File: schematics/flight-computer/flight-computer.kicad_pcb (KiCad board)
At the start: 4 copper layers, 80 x 80 mm, 141 parts, among them J101 BATT, J102 GPS, J103 TELEM, J104 Expansion Slot, J105 USB C, J106 SWD, J107 BLACKBOX, J301 BMI-S-201, Q101 BSS138, U101 STM32F405RGT6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

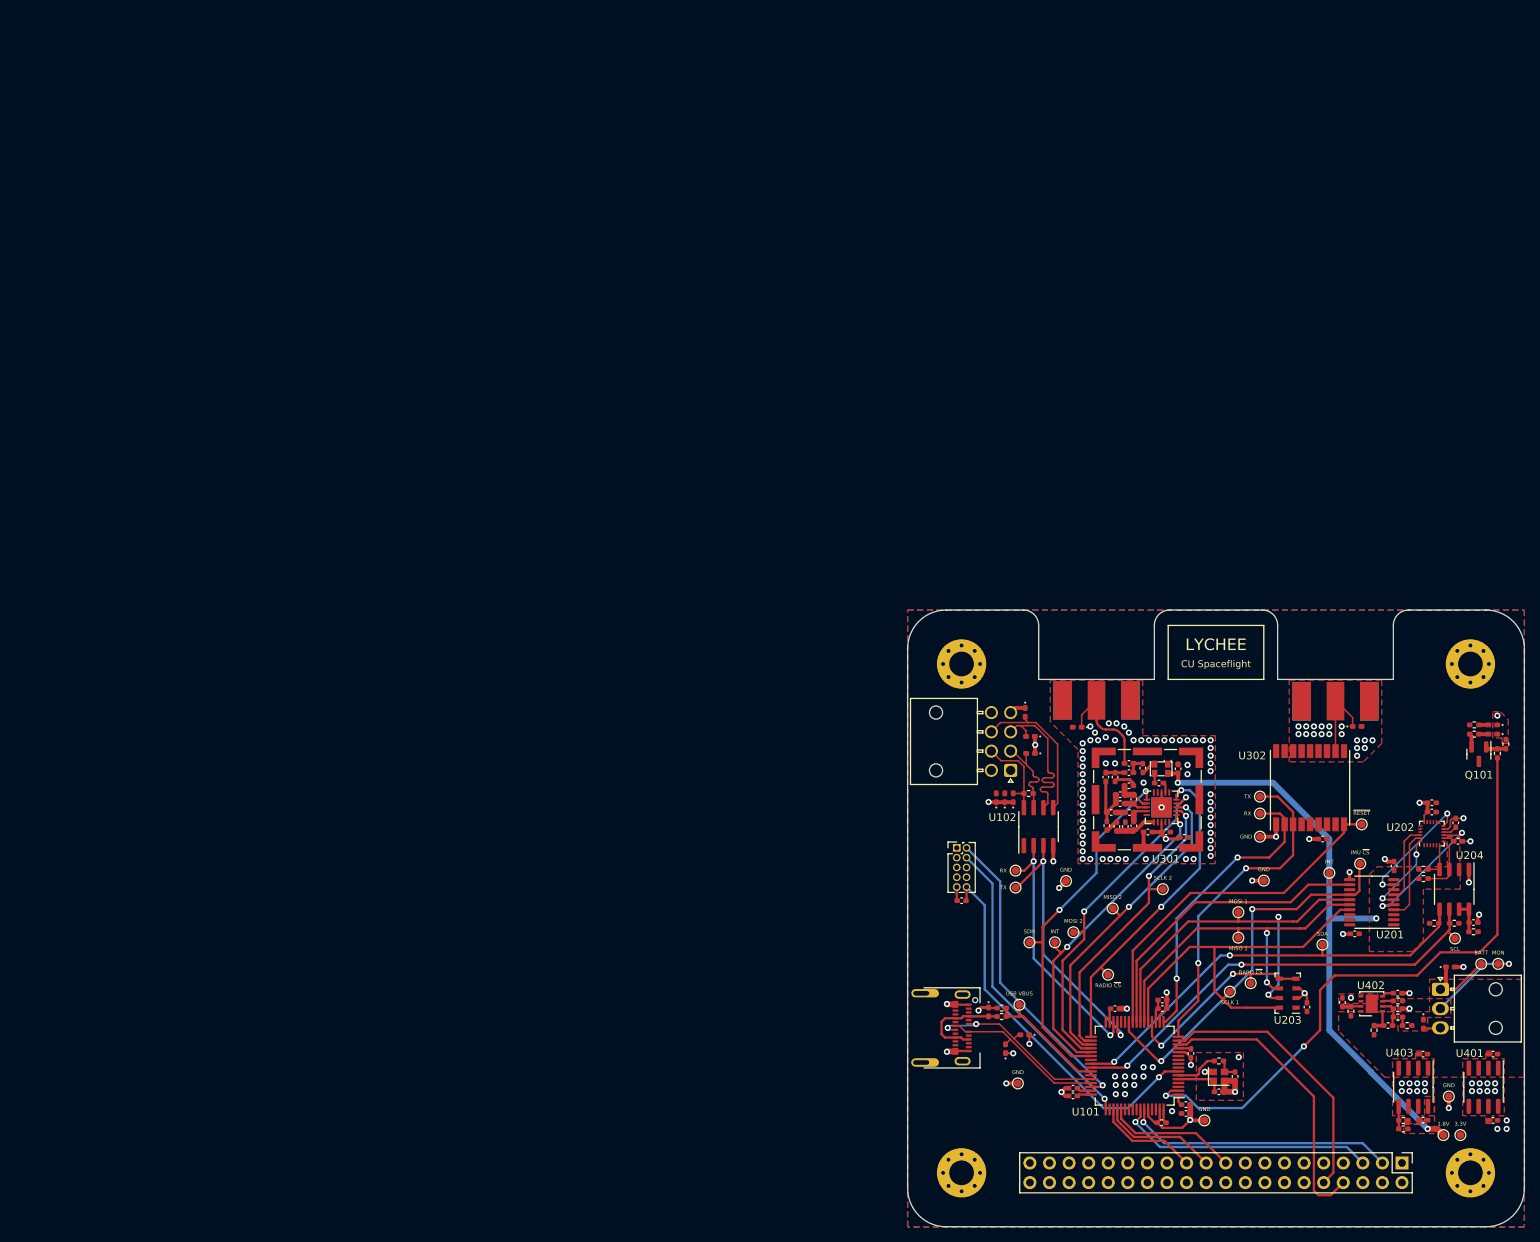
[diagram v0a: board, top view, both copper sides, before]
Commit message: Generate electrical docs
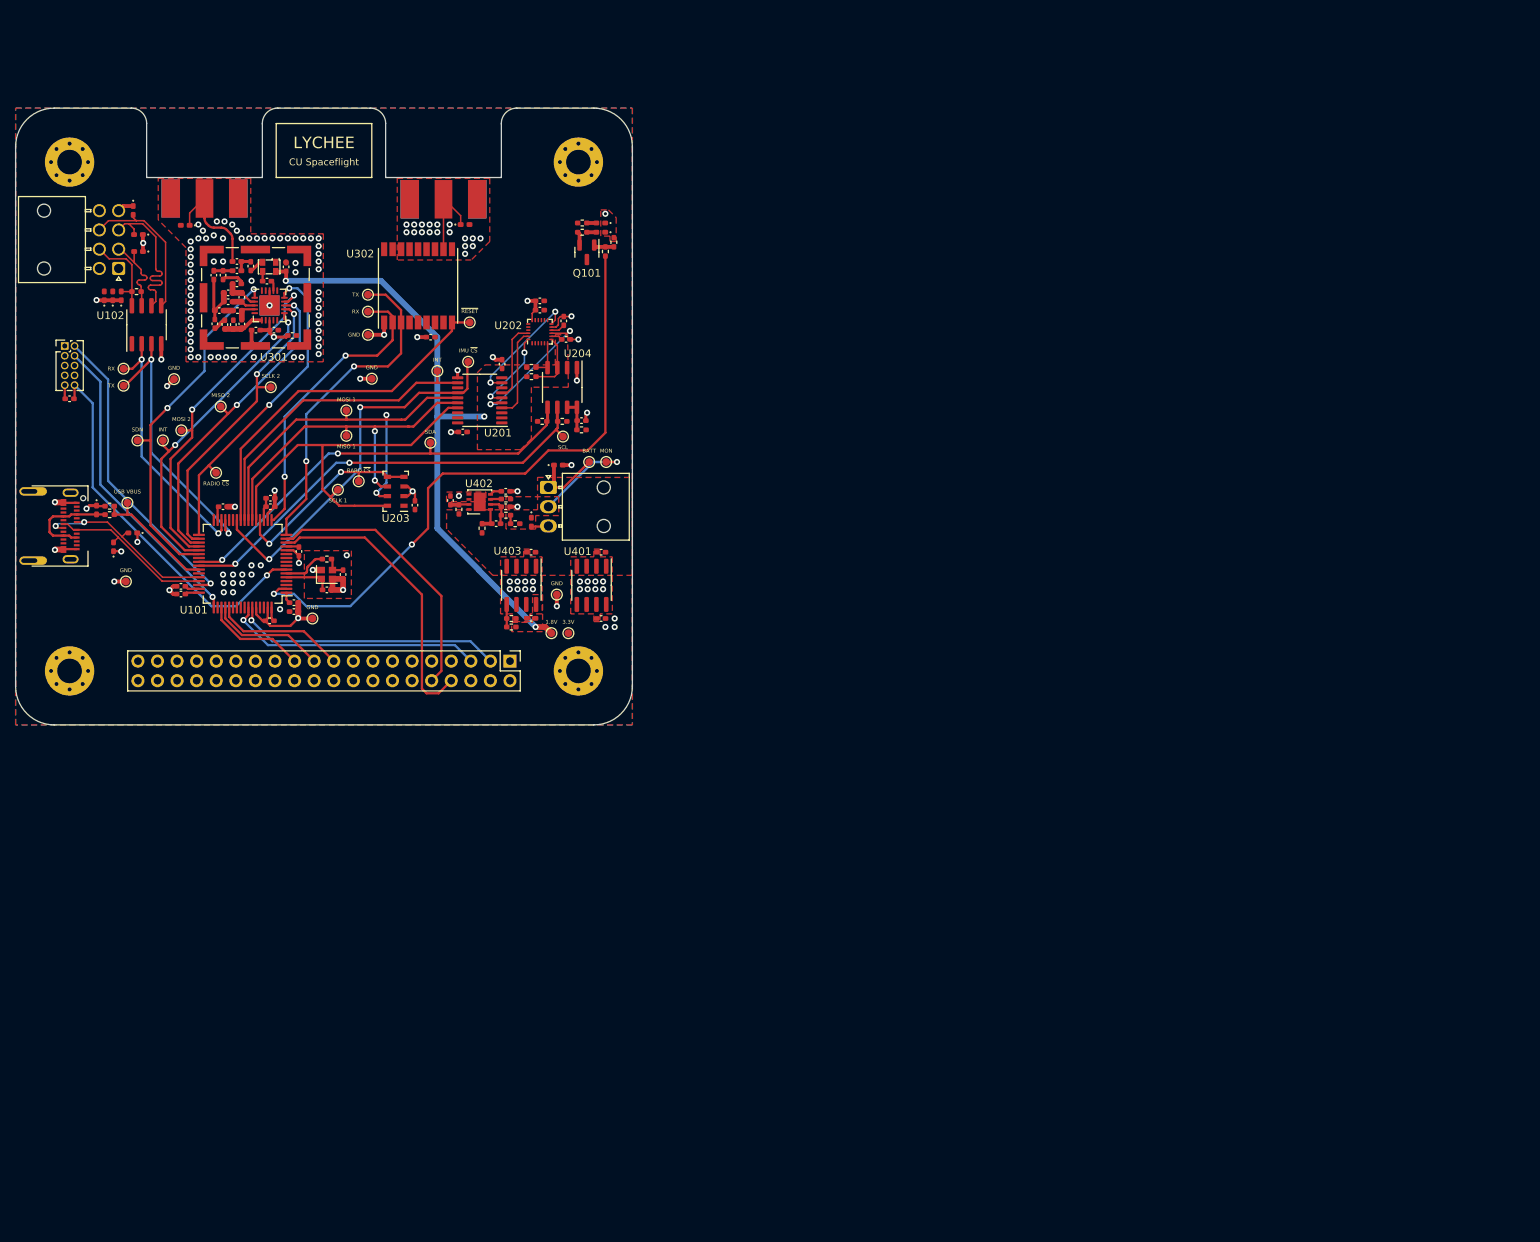
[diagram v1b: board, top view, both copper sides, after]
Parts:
- added G***: LOGO, Strix:CUSF_Logo, F.Cu at (230.5, 44.0)
- moved C101 132.8 mm to (86.0, 84.7)
- moved J101 132.8 mm to (122.1, 82.2)
- moved J107 132.8 mm to (66.4, 53.8)
- moved L306 132.8 mm to (82.3, 57.5)
- moved L307 132.8 mm to (80.6, 57.0)
- moved R108 132.8 mm to (68.7, 56.8)
- moved R406 132.8 mm to (117.3, 100.3)
- moved R407 132.8 mm to (117.3, 99.2)
- moved U203 132.8 mm to (102.3, 82.7)
- moved U302 132.8 mm to (105.2, 56.0)
- moved U402 132.8 mm to (113.2, 84.1)
- moved 1.8V 132.8 mm to (122.5, 101.1)
- moved 3.3V 132.8 mm to (124.7, 101.1)
- moved BARO ~{CS} 132.8 mm to (97.5, 81.4)
- moved BATT 132.8 mm to (127.4, 78.9)
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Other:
- board text added: "(To Blackbox)"
- board text added: "0"
- board text added: "0 mm"
- board text added: "0.0138 mm"
- board text added: "0.0152 mm"
- board text added: "0.02"
- board text added: "0.035 mm"
- board text added: "0.1500 mm / 0.1250 mm"
- board text added: "0.2104 mm"
- board text added: "0.3000 mm"
- board text added: "1"
- board text added: "1.065 mm"
- board text added: "1.6000 mm"
- board text added: "3.3"
- board text added: "3.8"
- board text added: "3v3"
- board text added: "4"
- board text added: "4.5"
- board text added: "80.0000 mm x 80.0000 mm"
- board text added: "B.Cu"
- board text added: "B.Mask"
- board text added: "B.Paste"
- board text added: "B.Silkscreen"
- board text added: "BOARD CHARACTERISTICS"
- board text added: "Blue"
- board text added: "Board Thickness:"
- board text added: "Board overall dimensions:"
- board text added: "Bottom Silk Screen"
- board text added: "Bottom Solder Mask"
- board text added: "Bottom Solder Paste"
- board text added: "Castellated pads:"
- board text added: "Color"
- board text added: "Copper Finish:"
- board text added: "Copper Layer Count:"
- board text added: "Dielectric 1"
- board text added: "Dielectric 2"
- board text added: "Dielectric 3"
- board text added: "Edge card connectors:"
- board text added: "Epsilon R"
- board text added: "F.Cu"
- board text added: "F.Mask"
- board text added: "F.Paste"
- board text added: "F.Silkscreen"
- board text added: "FR4"
- board text added: "Flight Computer"
- board text added: "GND"
- board text added: "Impedance Control:"
- board text added: "In1.Cu"
- board text added: "In2.Cu"
- board text added: "Layer Name"
- board text added: "Loss Tangent"
- board text added: "MISO"
- board text added: "MON"
- board text added: "MOSI"
- board text added: "Material"
- board text added: "Max 16V"
- board text added: "Min hole diameter:"
- board text added: "Min track/spacing:"
- board text added: "No"
- board text added: "None"
- board text added: "Not specified"
- board text added: "Pins marked with are GND."
- board text added: "Plated Board Edge:"
- board text added: "RX+"
- board text added: "RX-"
- board text added: "Rx"
- board text added: "SCA"
- board text added: "SCL"
- board text added: "SCLK"
- board text added: "TX+"
- board text added: "TX-"
- board text added: "Thickness (mm)"
- board text added: "Top Silk Screen"
- board text added: "Top Solder Mask"
- board text added: "Top Solder Paste"
- board text added: "Tx"
- board text added: "Type"
- board text added: "V+"
- board text added: "White"
- board text added: "copper"
- board text added: "core"
- board text added: "prepreg"

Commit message: Update layout doc
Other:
- board text added: "0.01 mm"
- board text added: "1.6062 mm"
- board text added: "GPS ANTENNA (SMA)"
- board text added: "HAL SnPb"
- board text added: "RADIO ANTENNA (SMA)"
- board text removed: "0.0138 mm"
- board text removed: "1.6000 mm"
- board text removed: "3.8"
- board text removed: "None"

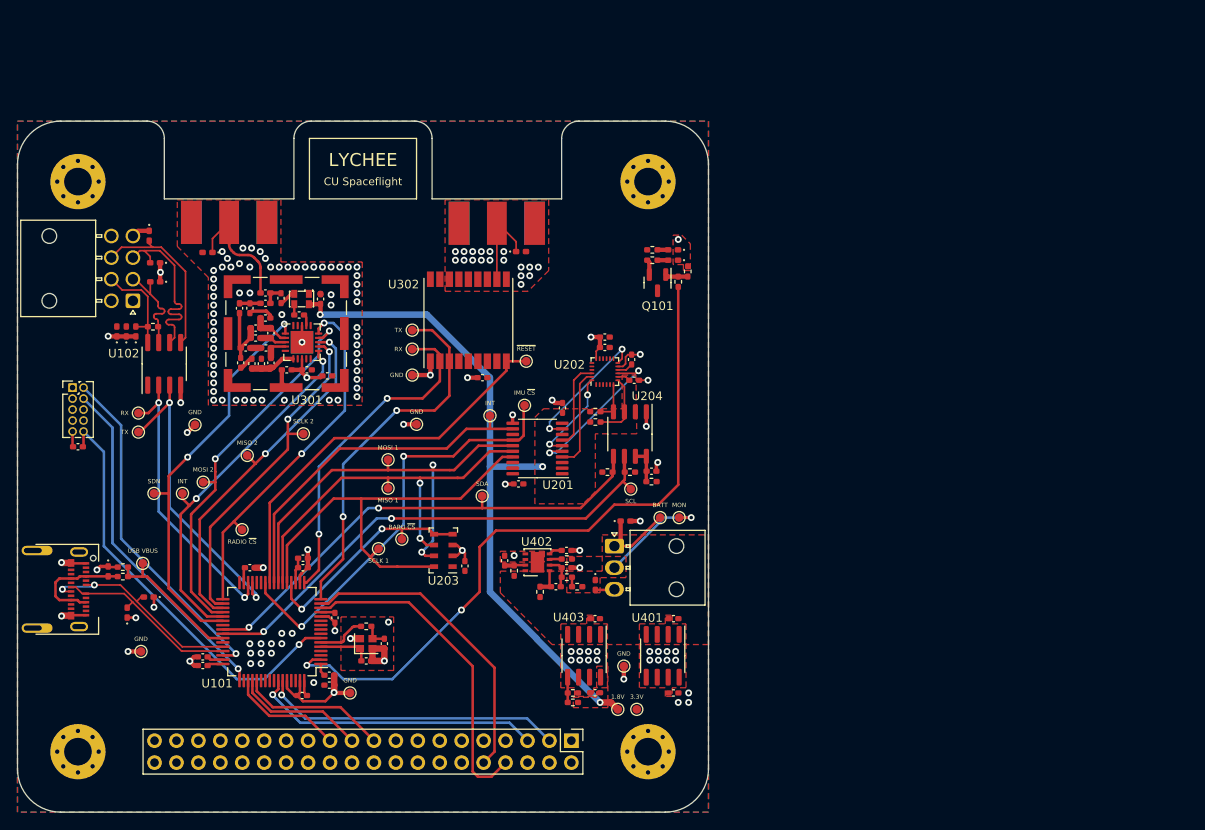
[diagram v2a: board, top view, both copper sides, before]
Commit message: Update PCB annotations and layout doc
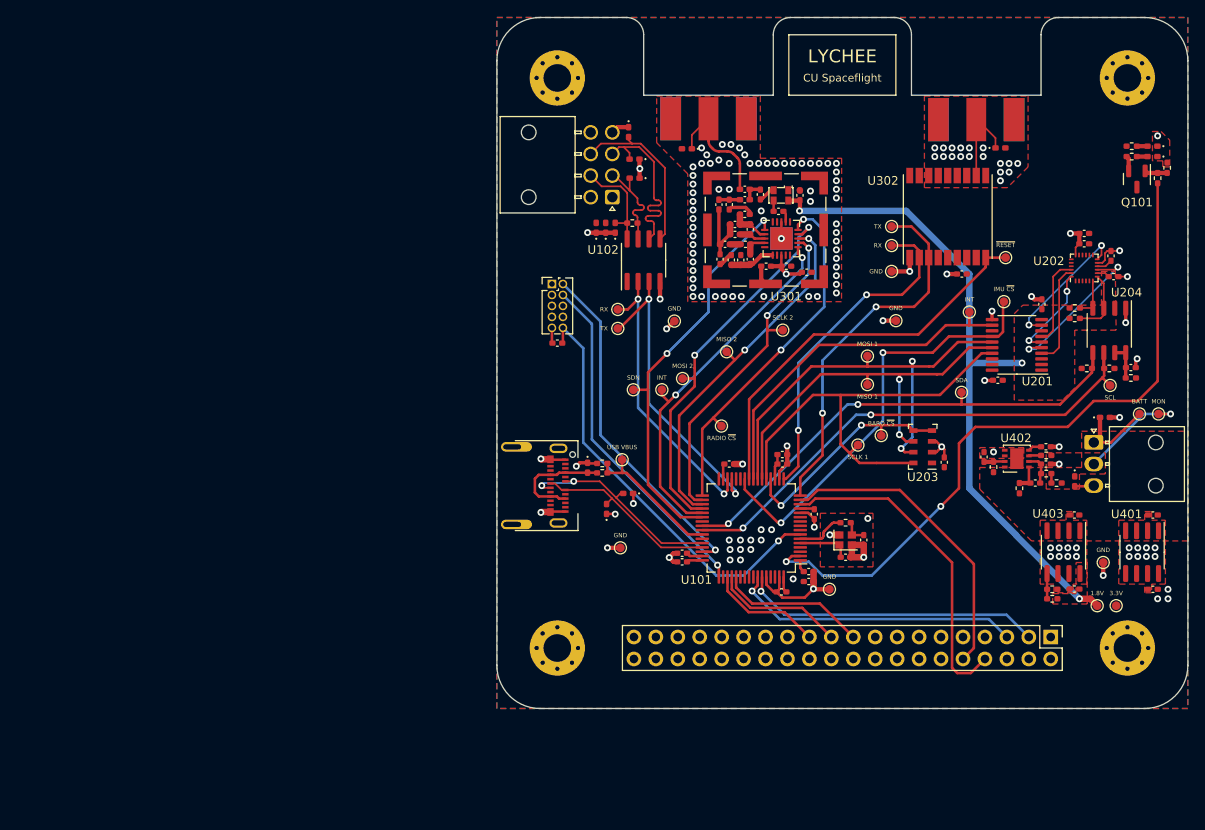
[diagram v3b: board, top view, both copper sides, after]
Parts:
- moved G*** 89.3 mm to (264.6, 126.6)
- moved C101 56.8 mm to (141.6, 72.7)
- moved C107 56.8 mm to (141.6, 71.6)
- moved C207 56.8 mm to (160.3, 72.5)
- moved C305 56.8 mm to (135.4, 42.7)
- moved C313 56.8 mm to (144.4, 50.5)
- moved C314 56.8 mm to (162.3, 50.7)
- moved C403 56.8 mm to (170.8, 74.9)
- moved D103 56.8 mm to (166.8, 36.1)
- moved GND 56.8 mm to (129.1, 56.1)
- moved J101 56.8 mm to (177.6, 70.2)
- moved L307 56.8 mm to (136.1, 45.0)
- moved R203 56.8 mm to (176.8, 61.6)
- moved R403 56.8 mm to (173.3, 74.9)
- moved R406 56.8 mm to (172.8, 88.3)
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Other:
- board text added: "1.6 mm"
- board text added: "80 mm x 80 mm"
- board text added: "RX"
- board text added: "SDA"
- board text added: "TX"
- board text removed: "1.6062 mm"
- board text removed: "3v3"
- board text removed: "80.0000 mm x 80.0000 mm"
- board text removed: "RX+"
- board text removed: "RX-"
- board text removed: "Rx"
- board text removed: "SCA"
- board text removed: "TX+"
- board text removed: "TX-"
- board text removed: "Tx"
